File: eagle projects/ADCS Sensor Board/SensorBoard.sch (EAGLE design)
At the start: 95 parts, among them J1 HDR_10_EZFET_DEBUGGER, J2 MTI-1_8428-11B1-RK-TP, Q1 BC850SMD, Q2 IRF7507TRPBF, U1 MSP430F5529IPN, U2 LMV321, U3 ADS7841E_2K5, U4 LMV321, U5 LMV321, Y1 32.768kHz, Y2 CSTCR4M00G15L99

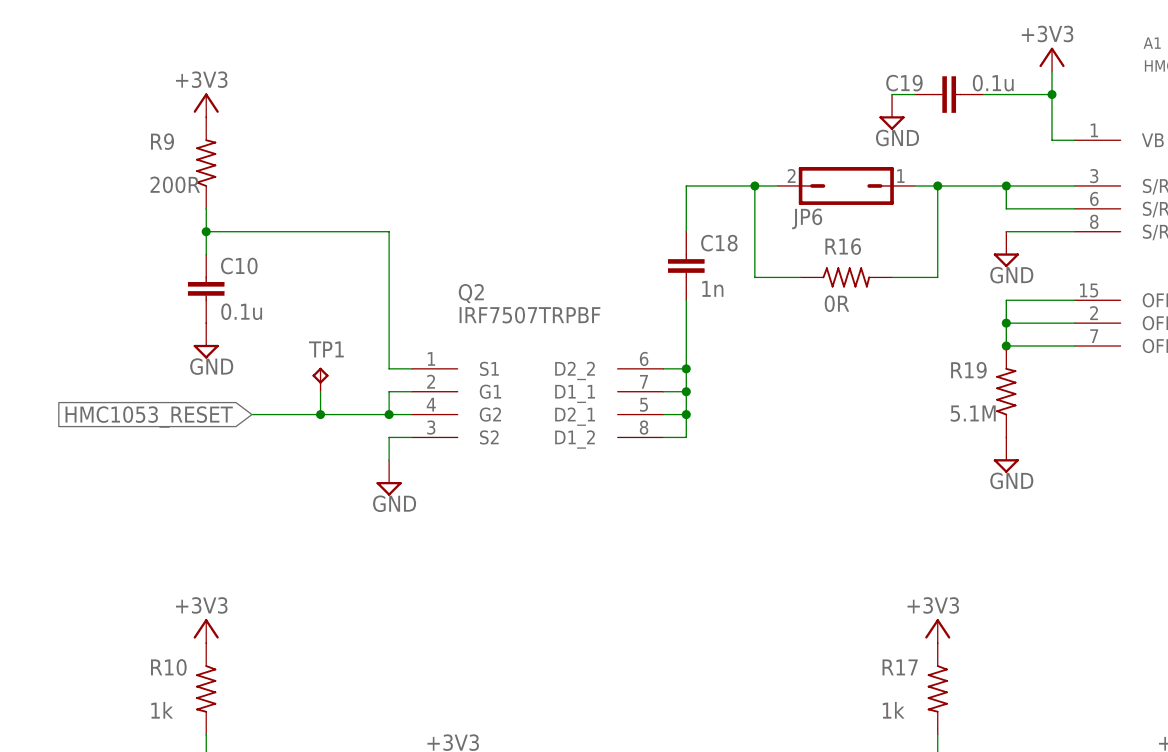
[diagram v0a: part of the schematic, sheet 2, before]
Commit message: Replaced obsolete transistor Q2
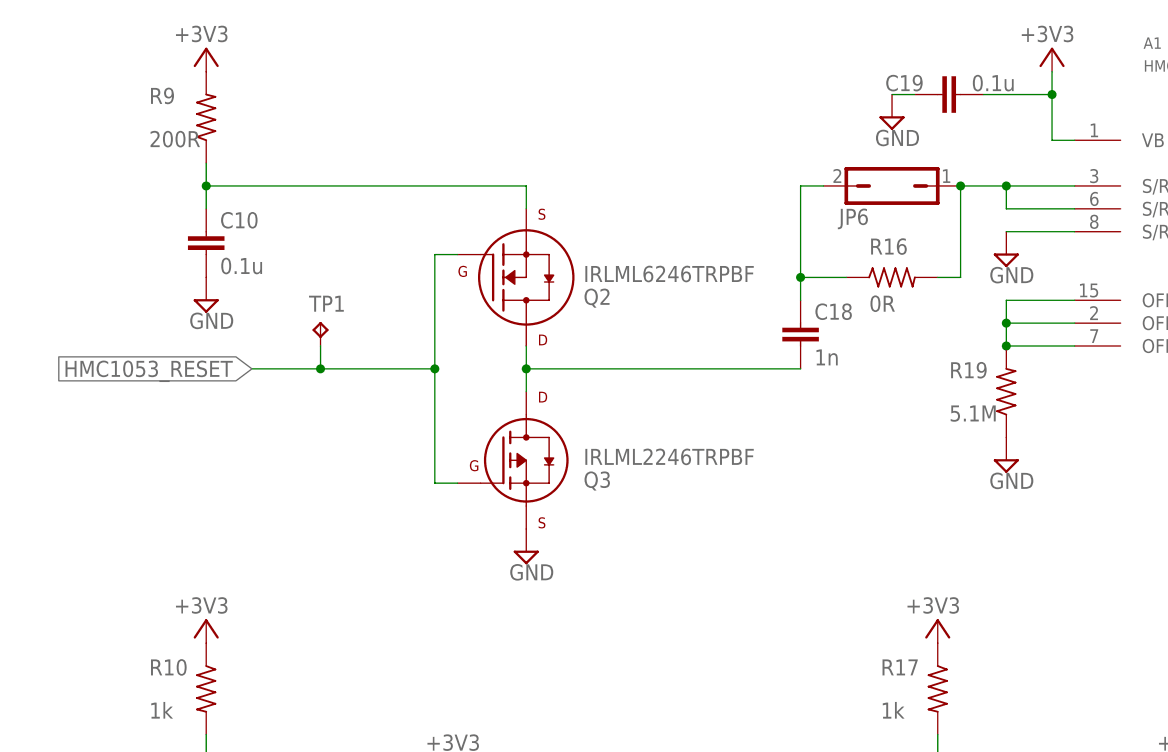
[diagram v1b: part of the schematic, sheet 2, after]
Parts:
- added Q3: IRLML2246TRPBF, my_library:IRLML2246TRPBF
- added R36: 10k, rcl:R-US_R0603
- C12, C13, C9: device resistor:C-EUC1206 -> rcl:C-EUC0805
- Q1: value BC850SMD -> PMV16XN; device transistor-npn:BC850SMD -> my_library:PMV16XN
- Q2: value IRF7507TRPBF -> IRLML6246TRPBF; device my_library:IRF7507TRPBF -> my_library:IRLML6246TRPBF
- R19, R9: device resistor:R-US_R1206 -> rcl:R-US_R0805
- R2, R3, R4, R5: device rcl:R-US_R0402 -> rcl:R-US_R0805
- R31, R32, R8: device rcl:R-US_R0603 -> rcl:R-US_R0805
- R6: device rcl:R-US_R0402 -> rcl:R-US_R0603
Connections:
- removed net N$38: C18.1, Q2.D1_1, Q2.D1_2, Q2.D2_1, Q2.D2_2
- new net N$9: C18.1, Q2.D, Q3.D
- net GND: now also Q1.S, Q3.S, R36.1; no longer Q1.E, Q2.S2
- net HMC1053_RESET: now also Q2.G, Q3.G; no longer Q2.G1, Q2.G2
- net MSP_OBC_RESET: now also Q1.G, R36.2; no longer Q1.B
- net N$39: now also Q2.S; no longer Q2.S1
- net RST/SBWTDIO: now also Q1.D; no longer Q1.C
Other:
- moved on the sheet: C10, C18, JP6, R16, R7, R9, TP1

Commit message: updated all libraries
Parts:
- removed JP5: (no value), my_library:PINHD-2X6
- added J3: HDR_2X5_GRPB052VWQS-RC, my_library:HDR_2X5_GRPB052VWQS-RC
- added J4: (no value), my_library:HDR_1X2_
- R2, R3, R31, R32, R4, R5, R8: device rcl:R-US_R0805 -> rcl:R-US_R0603
- renumbered JP1 to J8, JP2 to J5, JP3 to J6, JP4 to J7, JP7 to J11, JP8 to J9, JP9 to J10
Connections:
- removed net RESERVED_3: JP5.6, U1.P6.1/CB1/A1
- removed net RESERVED_4: JP5.8, U1.P6.0/CB0/A0
- net !CS!_SPEED_X: now also U1.P6.6/CB6/A6; no longer U1.P6.5/CB5/A5
- net !CS!_SPEED_Y: now also U1.P6.5/CB5/A5; no longer U1.P6.6/CB6/A6
- net !RST!_MTI: now also U1.P6.3/CB3/A3; no longer U1.PU.1/DM
- net +3V3: now also J3.7; no longer JP5.1
- net ACT_BRD_3V_PRESENT: now also J3.4; no longer JP5.7
- net ACT_BRD_5V_SHIFTED: now also J3.2; no longer JP5.5
- net MSP430_ACTIVE: now also J3.10, U1.P6.0/CB0/A0; no longer JP5.10, U1.P2.6/RTCCLK/DMAE0
- net MSP_OBC_RESET: now also J3.5; no longer JP5.9
- net RESERVED_1: now also J3.6, U1.P6.2/CB2/A2; no longer JP5.2, U1.P6.3/CB3/A3
- net RESERVED_2: now also J3.8, U1.P6.1/CB1/A1; no longer JP5.4, U1.P6.2/CB2/A2
- net SEN_BRD_5V_PRESENT: now also J3.9; no longer JP5.3
- net UCA0RXD: now also J3.1, J4.2; no longer JP5.12
- net UCA0TXD: now also J3.3, J4.1; no longer JP5.11
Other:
- moved on the sheet: LED1, R2, R3, R4, R5, R8

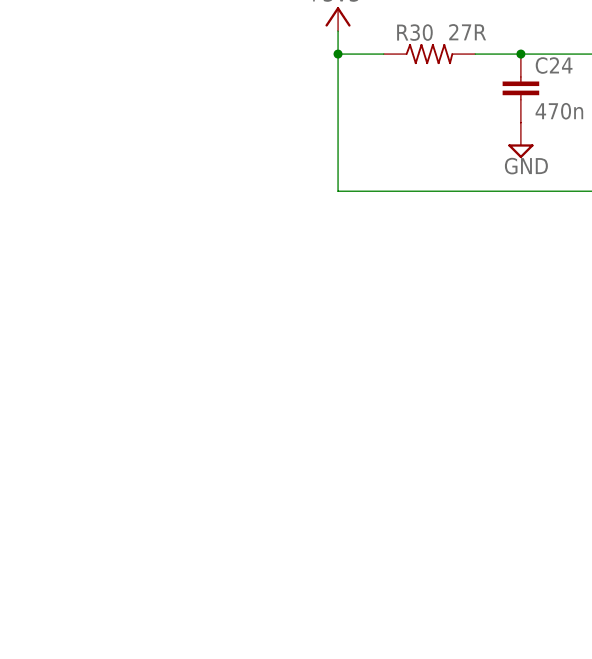
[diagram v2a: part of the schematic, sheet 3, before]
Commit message: Added mounting holes for sun sensor board, added standoff mounting holes to sensor board
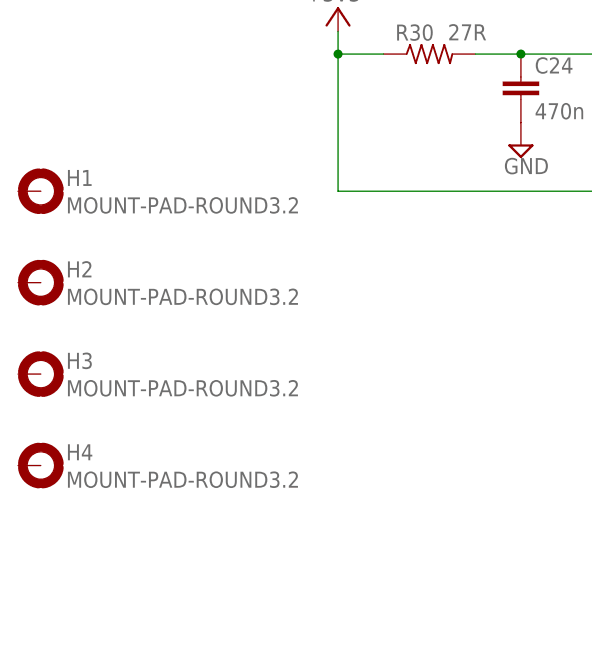
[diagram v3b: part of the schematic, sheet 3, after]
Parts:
- added H1, H2, H3, H4: MOUNT-PAD-ROUND3.2, holes:MOUNT-PAD-ROUND3.2
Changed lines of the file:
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@@
 <part name="+3V2" library="supply1" deviceset="+3V3" device=""/>
 <part name="J4" library="my_library" library_urn="urn:adsk.eagle:library:22876504" deviceset="HDR_1X2" device="_" package3d_urn="urn:adsk.eagle:package:24527019/1"/>
+<part name="H1" library="holes" library_urn="urn:adsk.eagle:library:237" deviceset="MOUNT-PAD-ROUND" device="3.2" package3d_urn="urn:adsk.eagle:package:14282/1"/>
+<part name="H2" library="holes" library_urn="urn:adsk.eagle:library:237" deviceset="MOUNT-PAD-ROUND" device="3.2" package3d_urn="urn:adsk.eagle:package:14282/1"/>
+<part name="H3" library="holes" library_urn="urn:adsk.eagle:library:237" deviceset="MOUNT-PAD-ROUND" device="3.2" package3d_urn="urn:adsk.eagle:package:14282/1"/>
+<part name="H4" library="holes" library_urn="urn:adsk.eagle:library:237" deviceset="MOUNT-PAD-ROUND" device="3.2" package3d_urn="urn:adsk.eagle:package:14282/1"/>
 </parts>
 <sheets>
@@
 <attribute name="NAME" x="100.33" y="123.19" size="1.778" layer="95"/>
 </instance>
+<instance part="H1" gate="G$1" x="30.48" y="121.92" smashed="yes">
+<attribute name="NAME" x="33.274" y="122.5042" size="1.778" layer="95"/>
+<attribute name="VALUE" x="33.274" y="119.4562" size="1.778" layer="96"/>
+</instance>
+<instance part="H2" gate="G$1" x="30.48" y="111.76" smashed="yes">
+<attribute name="NAME" x="33.274" y="112.3442" size="1.778" layer="95"/>
+<attribute name="VALUE" x="33.274" y="109.2962" size="1.778" layer="96"/>
+</instance>
+<instance part="H3" gate="G$1" x="30.48" y="101.6" smashed="yes">
+<attribute name="NAME" x="33.274" y="102.1842" size="1.778" layer="95"/>
+<attribute name="VALUE" x="33.274" y="99.1362" size="1.778" layer="96"/>
+</instance>
+<instance part="H4" gate="G$1" x="30.48" y="91.44" smashed="yes">
+<attribute name="NAME" x="33.274" y="92.0242" size="1.778" layer="95"/>
+<attribute name="VALUE" x="33.274" y="88.9762" size="1.778" layer="96"/>
+</instance>
 </instances>

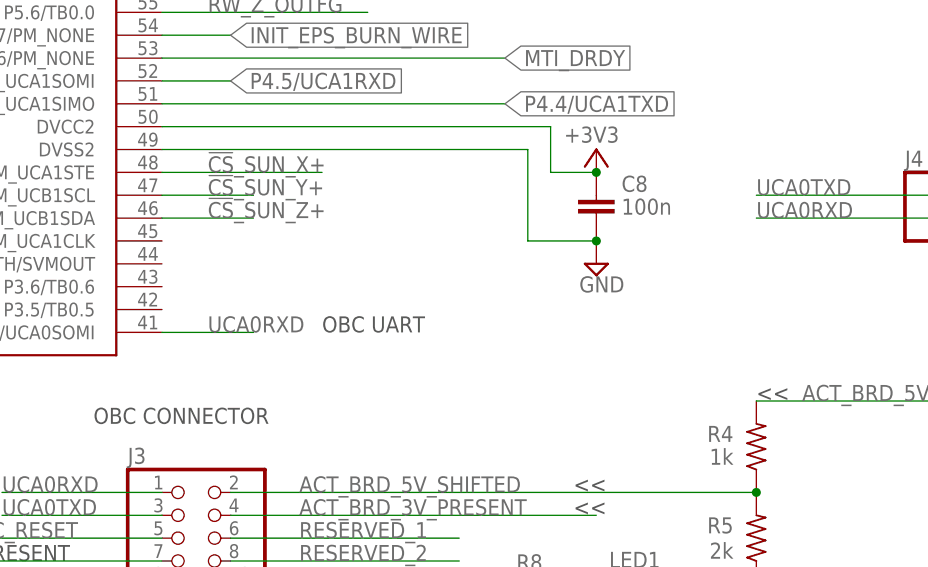
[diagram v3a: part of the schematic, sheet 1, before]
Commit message: sensor board updates for rev b
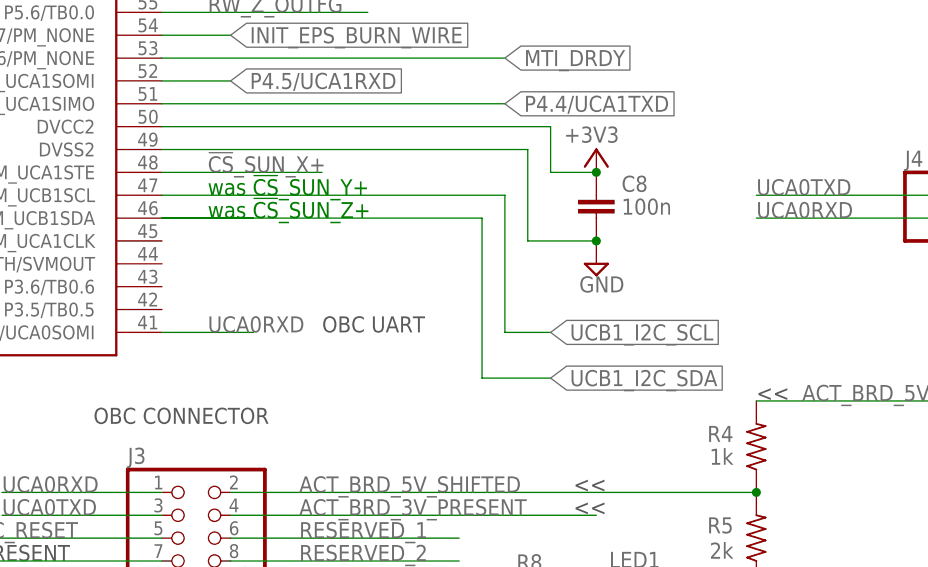
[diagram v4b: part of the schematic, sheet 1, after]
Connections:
- new net UCB1_I2C_SCL: U1.P4.2/PM_UCB1SOMI/PM_UCB1SCL
- new net UCB1_I2C_SDA: U1.P4.1/PM_UCB1SIMO/PM_UCB1SDA
- net !CS!_SUN_Y+: no longer U1.P4.2/PM_UCB1SOMI/PM_UCB1SCL
- net !CS!_SUN_Z+: no longer U1.P4.1/PM_UCB1SIMO/PM_UCB1SDA
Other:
- note added: "was !CS!_SUN_Y+"
- note added: "was !CS!_SUN_Z+"
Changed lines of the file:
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@@
 <schematic xreflabel="%F%N" xrefpart="/%S.%C%R">
 <attributes>
+<attribute name="REV" value="B"/>
 </attributes>
 <variantdefs>
@@
 <text x="218.44" y="53.34" size="1.778" layer="97">&lt;&lt;</text>
 <text x="137.16" y="48.26" size="1.778" layer="97">SEN_BRD_3V_PRESENT</text>
+<text x="177.8" y="88.9" size="1.778" layer="91">was !CS!_SUN_Y+</text>
+<text x="177.8" y="86.36" size="1.778" layer="91">was !CS!_SUN_Z+</text>
 </plain>
 <instances>
@@
 <label x="27.94" y="190.5" size="1.778" layer="95" grouprefs="Z+_SUN_SENSOR_CONNECTOR"/>
 </segment>
-<segment>
-<wire x1="172.72" y1="86.36" x2="182.88" y2="86.36" width="0.1524" layer="91"/>
-<pinref part="U1" gate="G$1" pin="P4.1/PM_UCB1SIMO/PM_UCB1SDA"/>
-<label x="177.8" y="86.36" size="1.778" layer="95"/>
-</segment>
 </net>
 <net name="!CS!_SUN_Y+" class="0">
@@
 <wire x1="55.88" y1="53.34" x2="22.86" y2="53.34" width="0.1524" layer="91" grouprefs="ACTUATOR_BOARD_CONNECTORS"/>
 <pinref part="J5" gate="A" pin="3"/>
-</segment>
-<segment>
-<wire x1="172.72" y1="88.9" x2="182.88" y2="88.9" width="0.1524" layer="91"/>
-<pinref part="U1" gate="G$1" pin="P4.2/PM_UCB1SOMI/PM_UCB1SCL"/>
-<label x="177.8" y="88.9" size="1.778" layer="95"/>
 </segment>
 </net>
@@
 </segment>
 </net>
+<net name="UCB1_I2C_SCL" class="0">
+<segment>
+<pinref part="U1" gate="G$1" pin="P4.2/PM_UCB1SOMI/PM_UCB1SCL"/>
+<wire x1="172.72" y1="88.9" x2="210.82" y2="88.9" width="0.1524" layer="91"/>
+<wire x1="210.82" y1="88.9" x2="210.82" y2="73.66" width="0.1524" layer="91"/>
+<wire x1="210.82" y1="73.66" x2="215.9" y2="73.66" width="0.1524" layer="91"/>
+<label x="215.9" y="73.66" size="1.778" layer="95" xref="yes"/>
+</segment>
+</net>
+<net name="UCB1_I2C_SDA" class="0">
+<segment>
+<wire x1="172.72" y1="86.36" x2="182.88" y2="86.36" width="0.1524" layer="91"/>
+<pinref part="U1" gate="G$1" pin="P4.1/PM_UCB1SIMO/PM_UCB1SDA"/>
+<wire x1="172.72" y1="86.36" x2="208.28" y2="86.36" width="0.1524" layer="91"/>
+<wire x1="208.28" y1="86.36" x2="208.28" y2="68.58" width="0.1524" layer="91"/>
+<wire x1="208.28" y1="68.58" x2="215.9" y2="68.58" width="0.1524" layer="91"/>
+<label x="215.9" y="68.58" size="1.778" layer="95" xref="yes"/>
+</segment>
+</net>
